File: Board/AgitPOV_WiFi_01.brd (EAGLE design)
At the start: 37.2 x 67.7 mm, 41 parts, among them U1 MMA8452Q

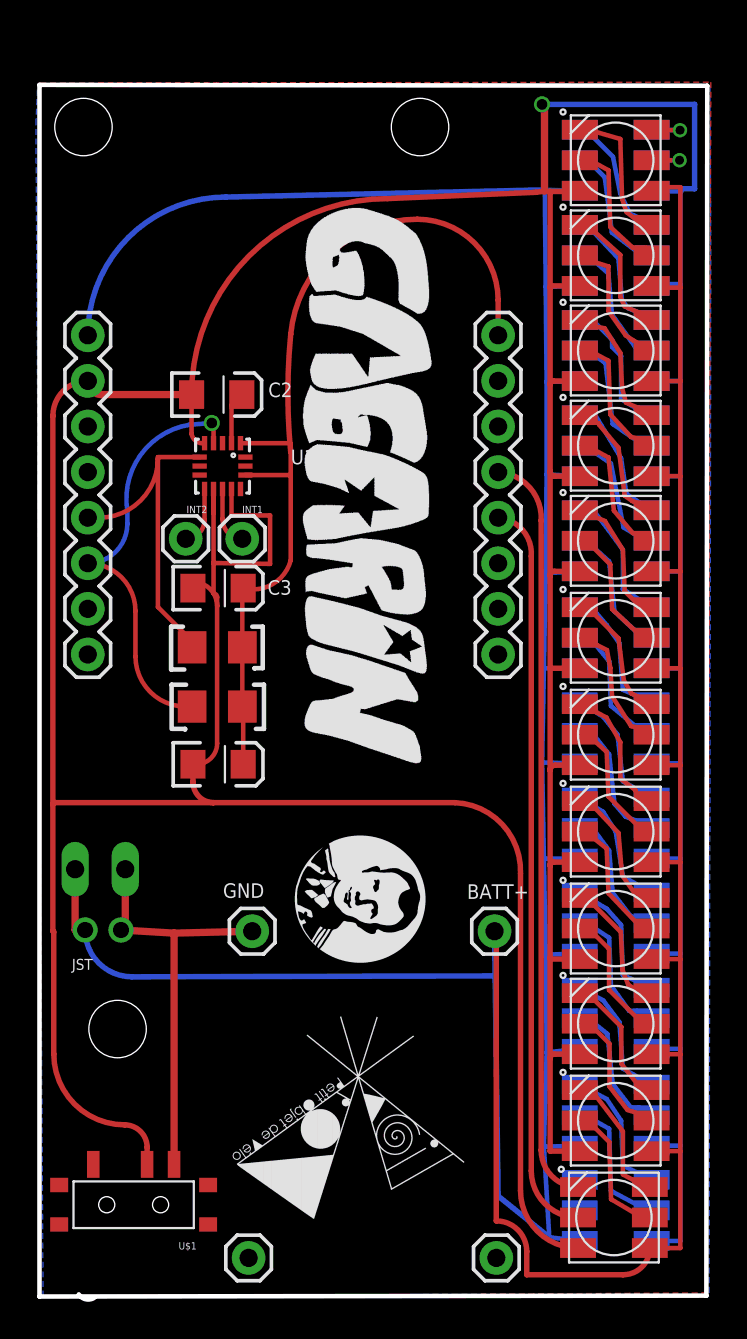
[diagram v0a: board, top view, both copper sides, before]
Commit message: Ajustement pour le tableau des caractères spéciaux
Nouveau board
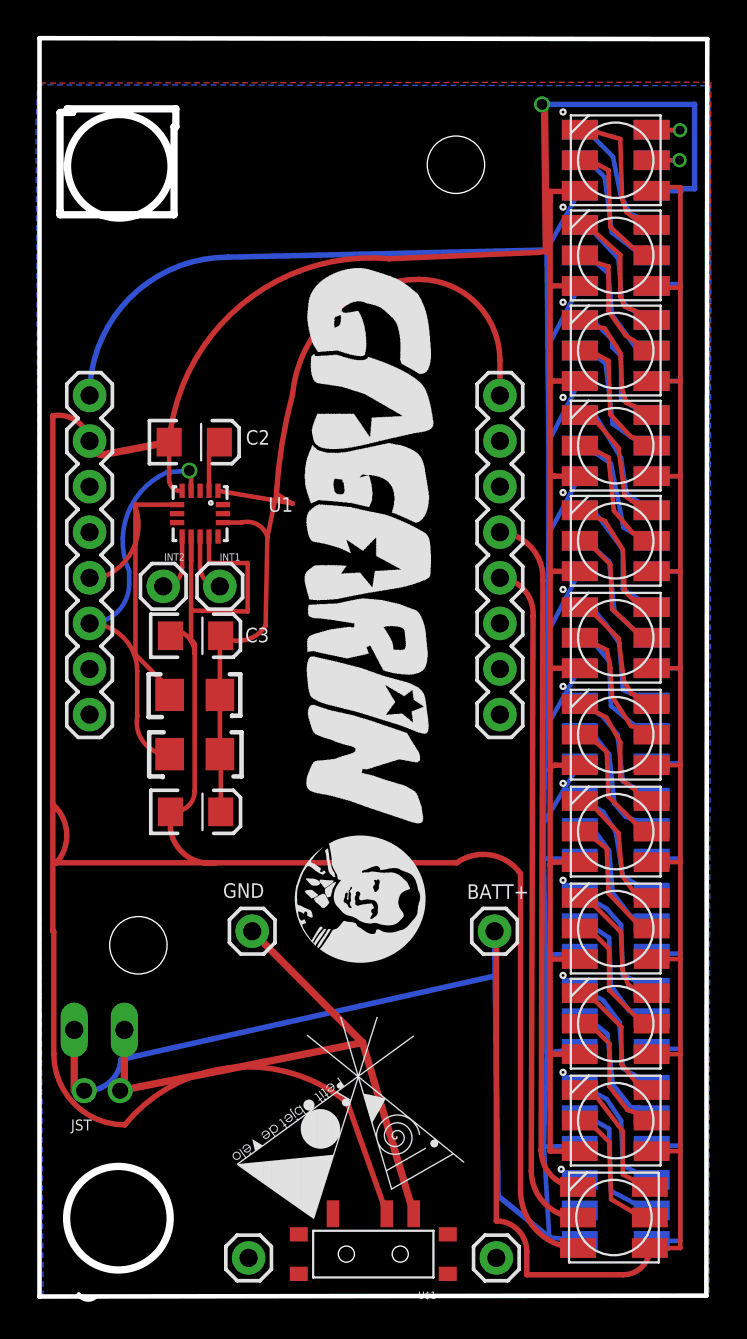
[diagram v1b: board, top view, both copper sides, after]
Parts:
- moved U$1 13.6 mm to (18.9, 2.70)
- moved BATT 8.95 mm to (4.96, 15.2)
- moved JST 8.95 mm to (3.85, 11.8)
- moved WEMOS1 3.35 mm to (26.0, 32.8)
- moved WEMOS2 3.35 mm to (3.14, 50.5)
- moved R1 2.93 mm to (9.00, 33.9)
- moved C1 2.93 mm to (9.05, 27.3)
- moved C2 2.93 mm to (8.98, 47.9)
- moved C3 2.93 mm to (9.05, 37.1)
- moved INT1 2.93 mm to (10.4, 39.9)
- moved INT2 2.93 mm to (7.25, 39.9)
- moved R2 2.93 mm to (9.00, 30.6)
- moved U1 2.93 mm to (9.30, 44.0)
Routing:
- net GND: track 332.9 -> 357.4 mm
- net ENTREEGND: track 23.8 -> 36.1 mm
- net 5V: track 262.4 -> 272.4 mm
- net N$4: track 41.6 -> 38.2 mm
- net N$2: track 40.8 -> 37.4 mm
- net +3.3V: track 49.2 -> 51.2 mm
- net SCL: track 22.8 -> 21.3 mm
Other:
- board size 37.2 x 67.7 mm -> 37.2 x 70.3 mm
